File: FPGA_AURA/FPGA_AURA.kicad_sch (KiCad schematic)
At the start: 0 parts

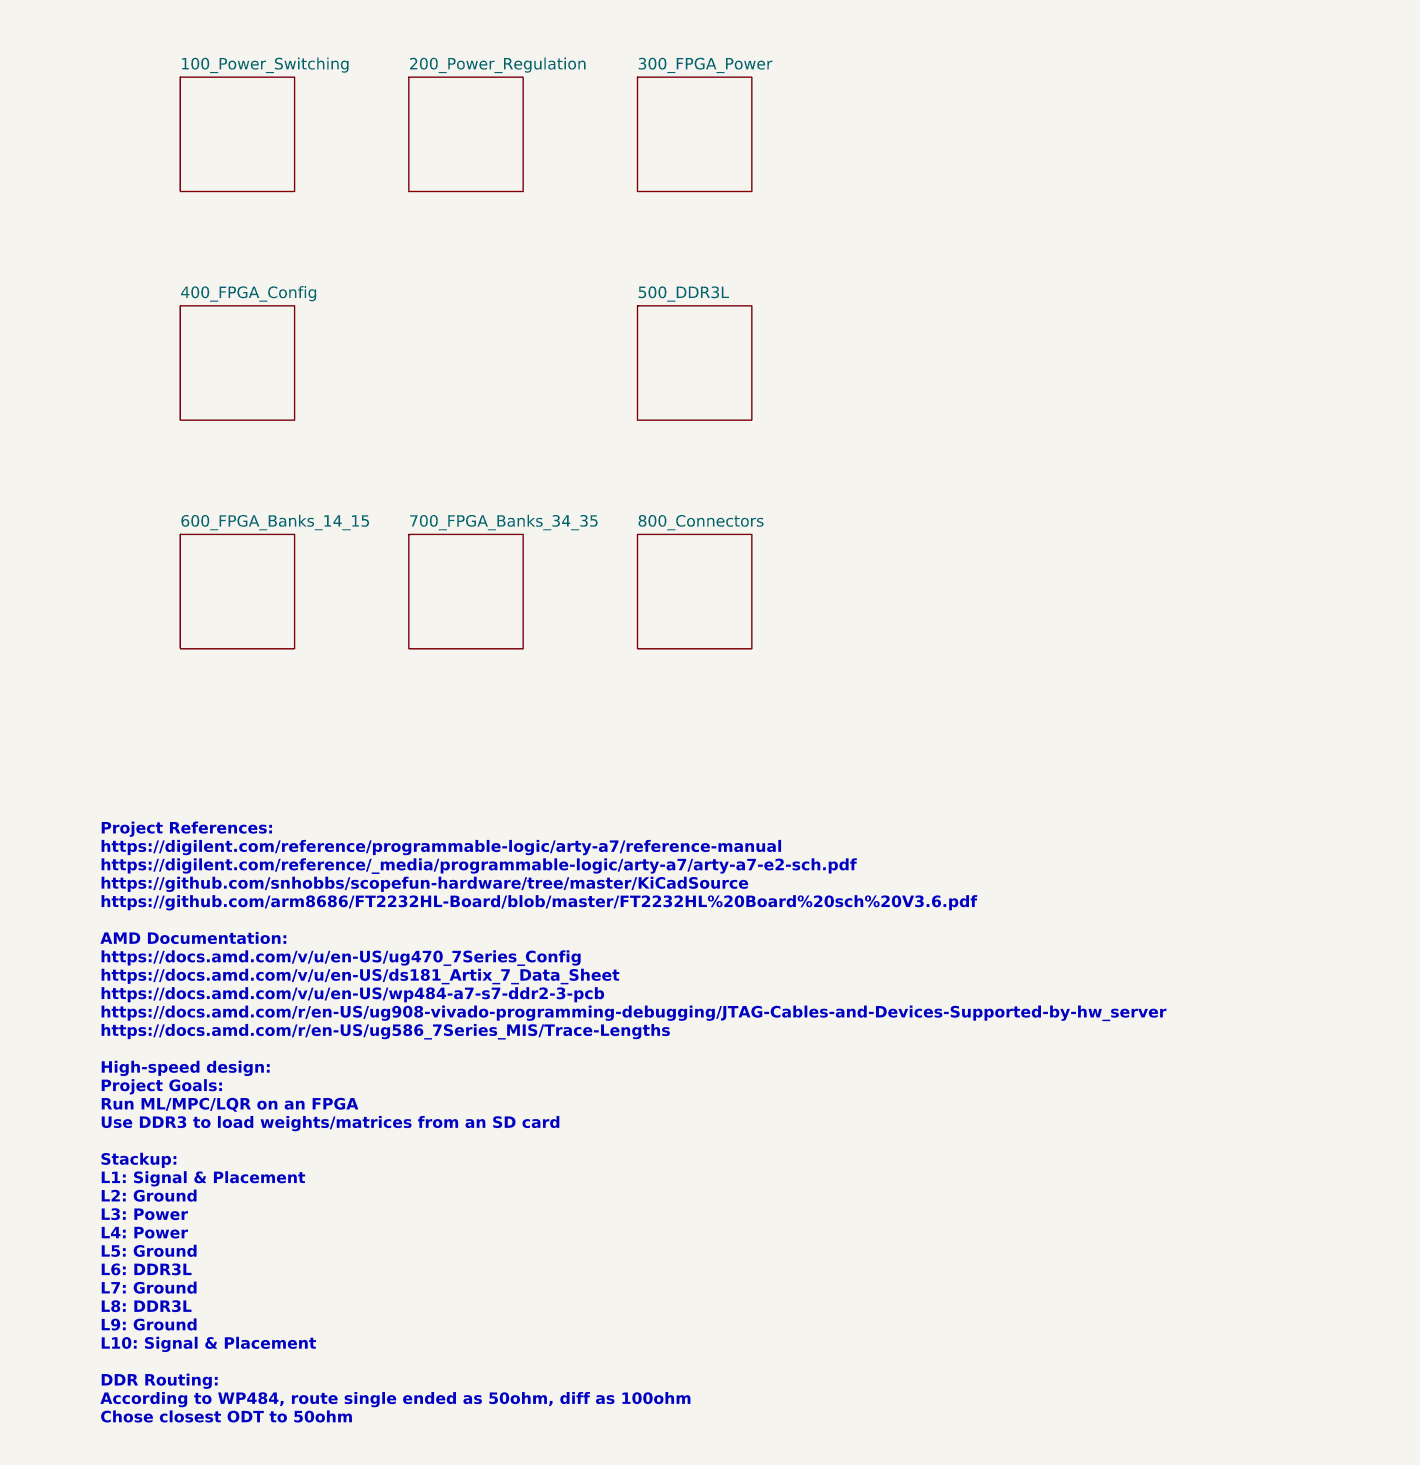
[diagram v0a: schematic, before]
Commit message: Started DDR routing with new layout.
All impedances setup for PCBway 8 layer stack-up.  Routing issues with the DQ lanes still to be resolved.
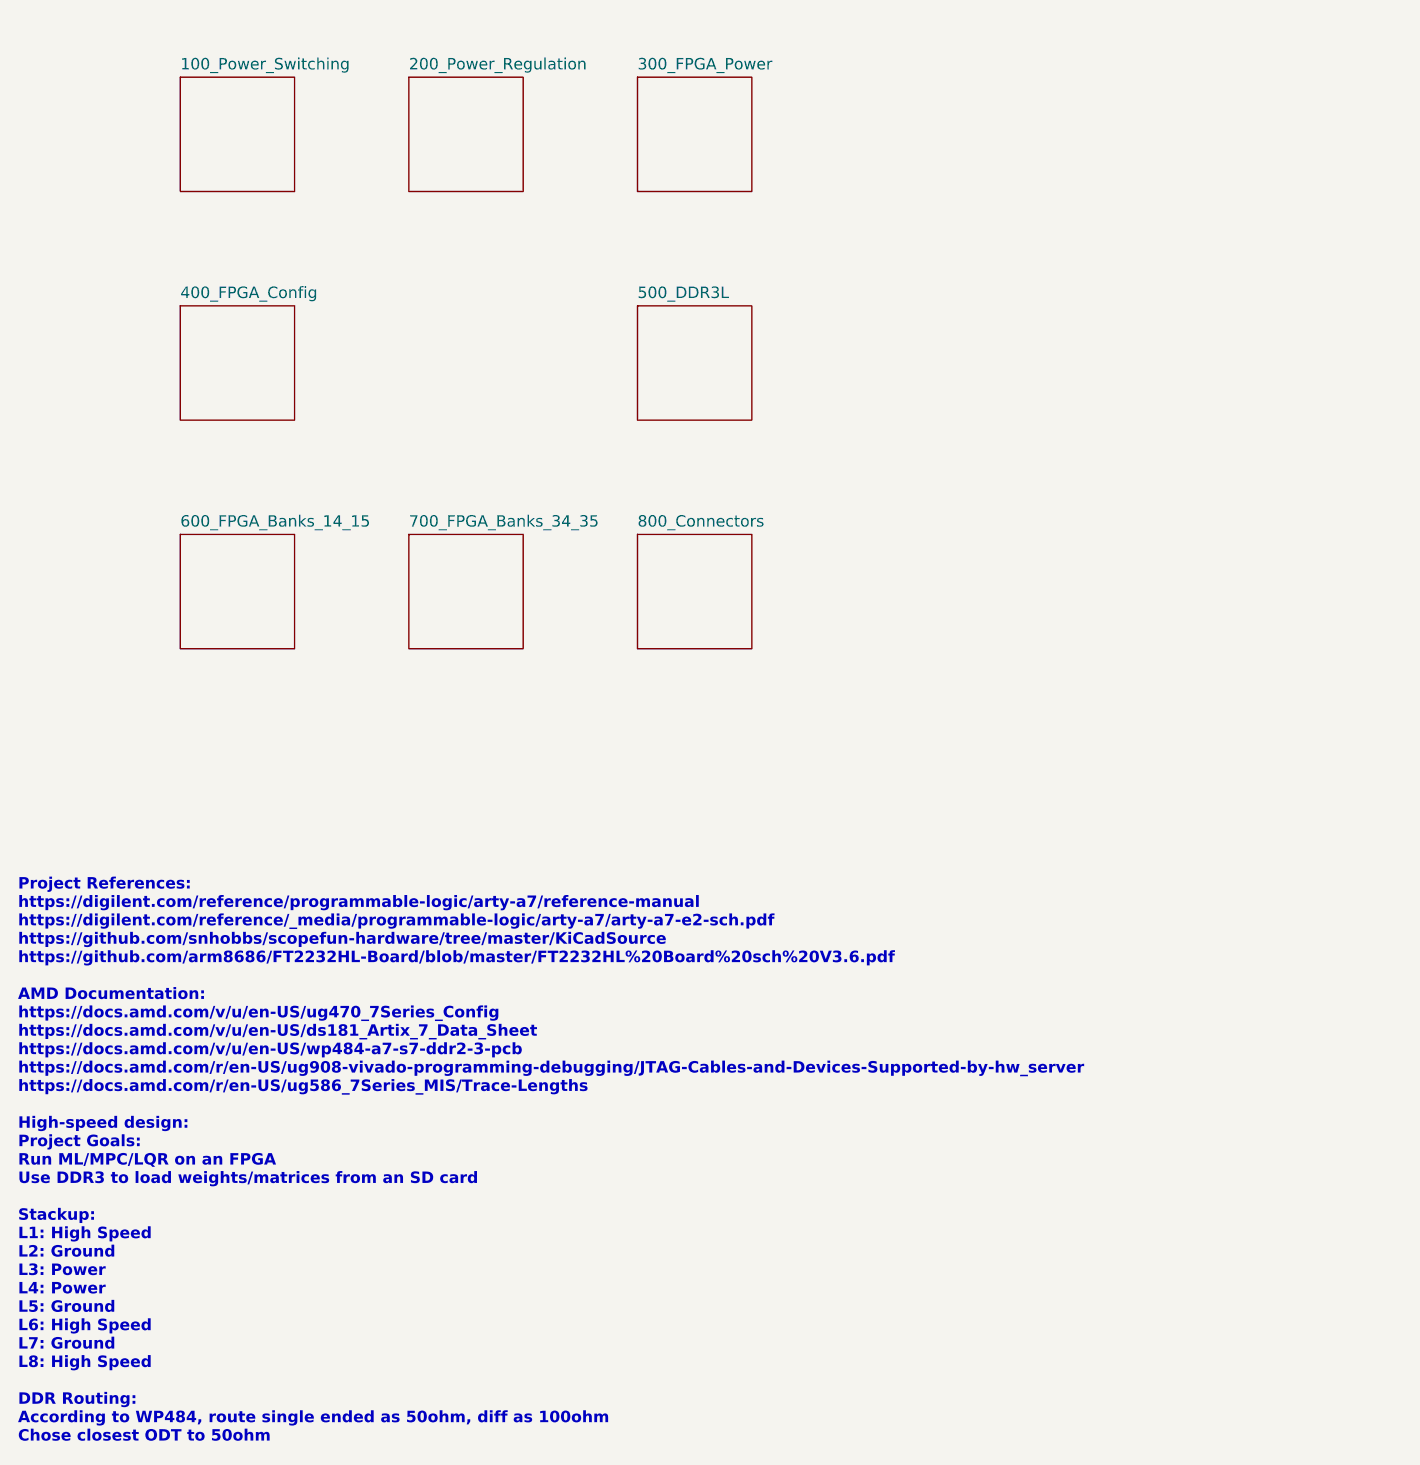
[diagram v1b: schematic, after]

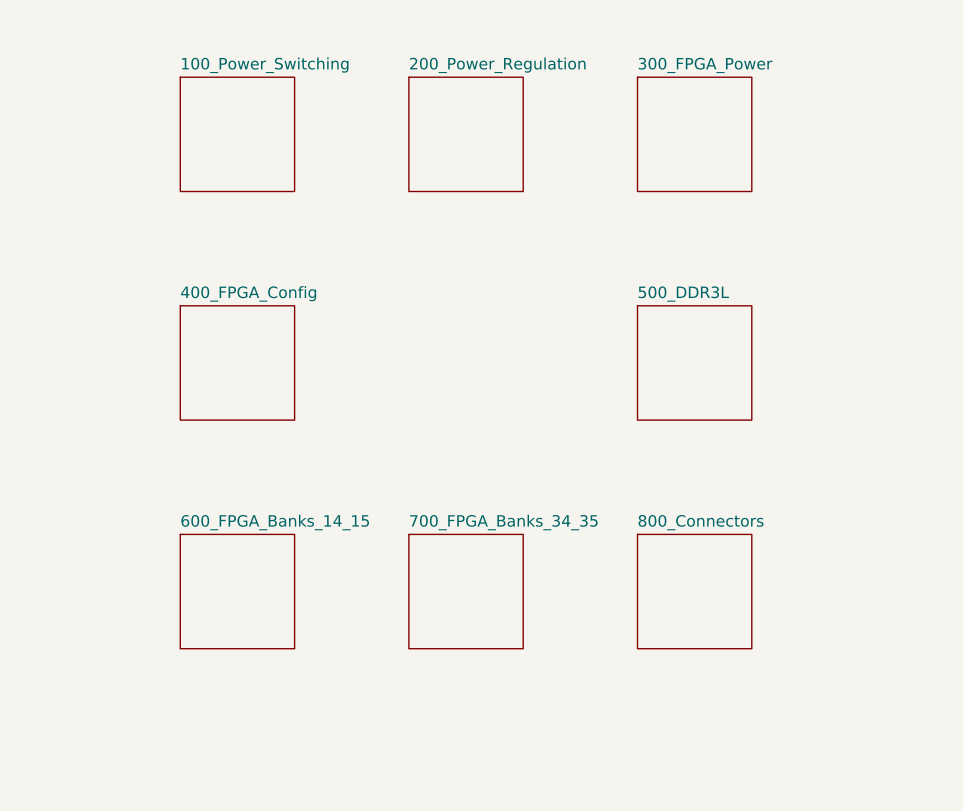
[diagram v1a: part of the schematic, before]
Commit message: DDR3 Routing complete on 3 layers, top layer left.
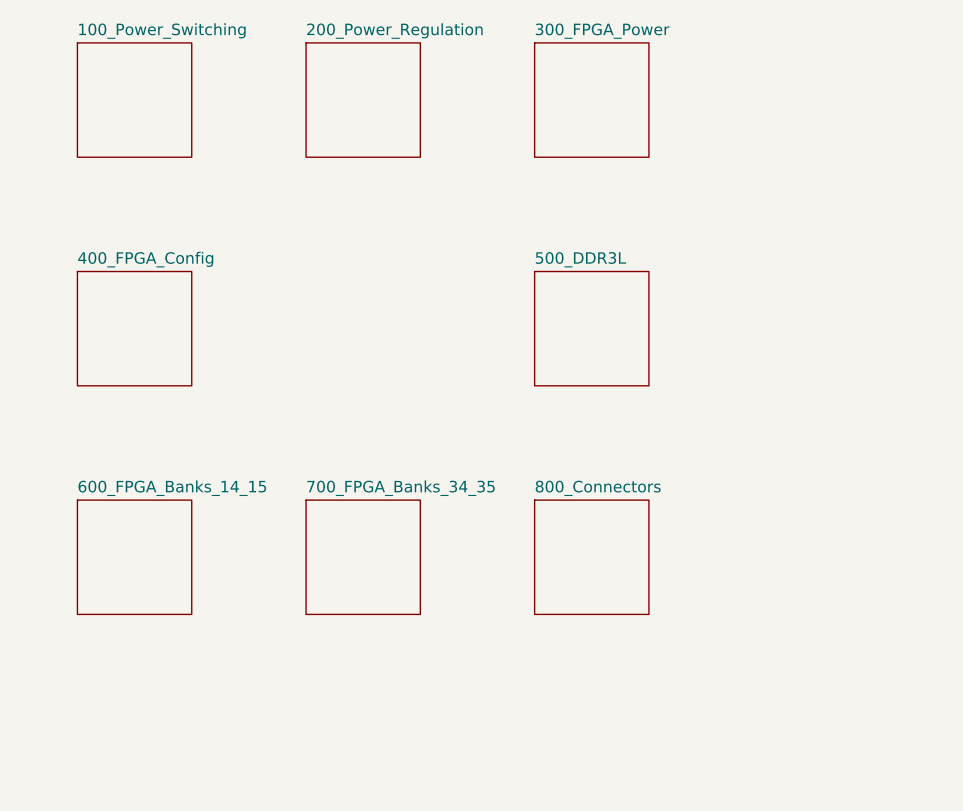
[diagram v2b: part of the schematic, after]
